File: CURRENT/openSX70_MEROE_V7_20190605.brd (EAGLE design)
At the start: 95.9 x 27.9 mm, 43 parts, among them J1 687106183722, Q1 5.8A/30V/35mΩ, Q2 5.8A/30V/35mΩ, U1 ATMEGA328P_TQFP, U2 TPS79501DCQ, Y1 CSTCE8M00G52Z-R0

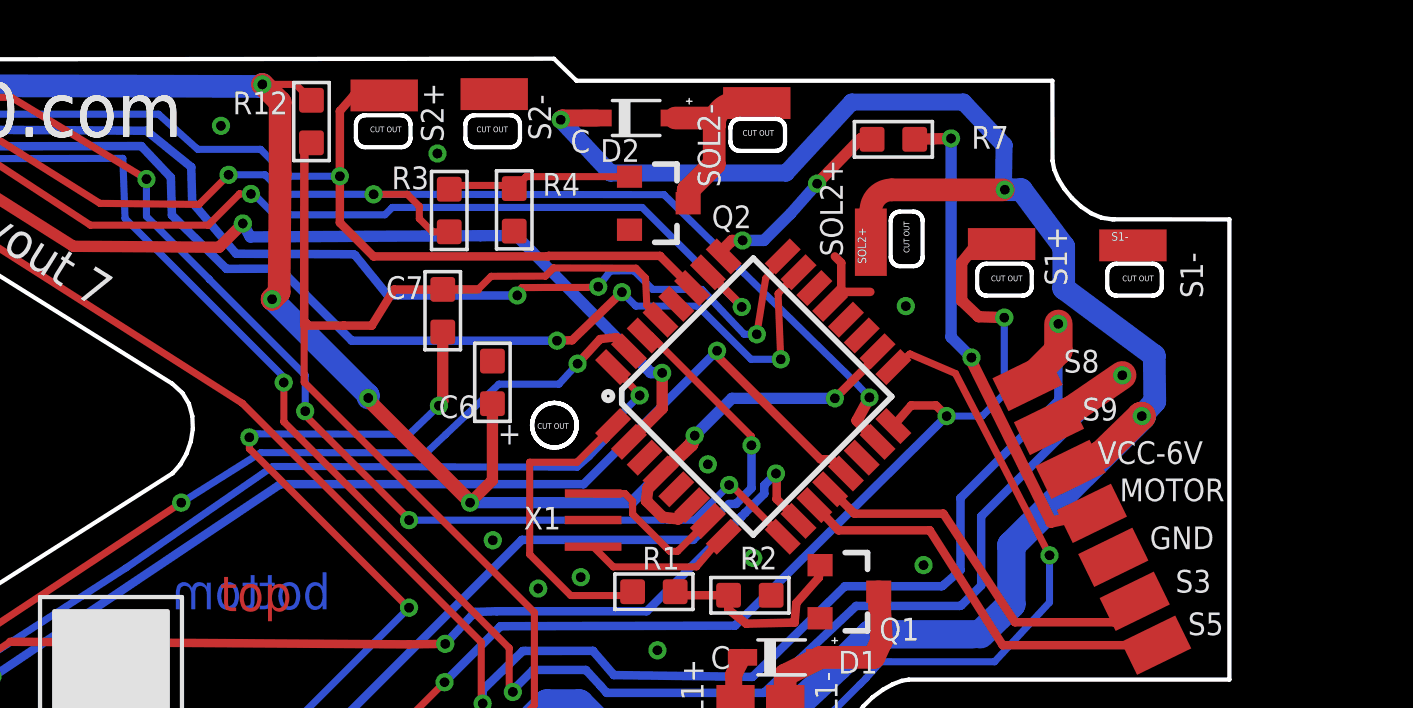
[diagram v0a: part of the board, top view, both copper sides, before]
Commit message: adding decoupling caps
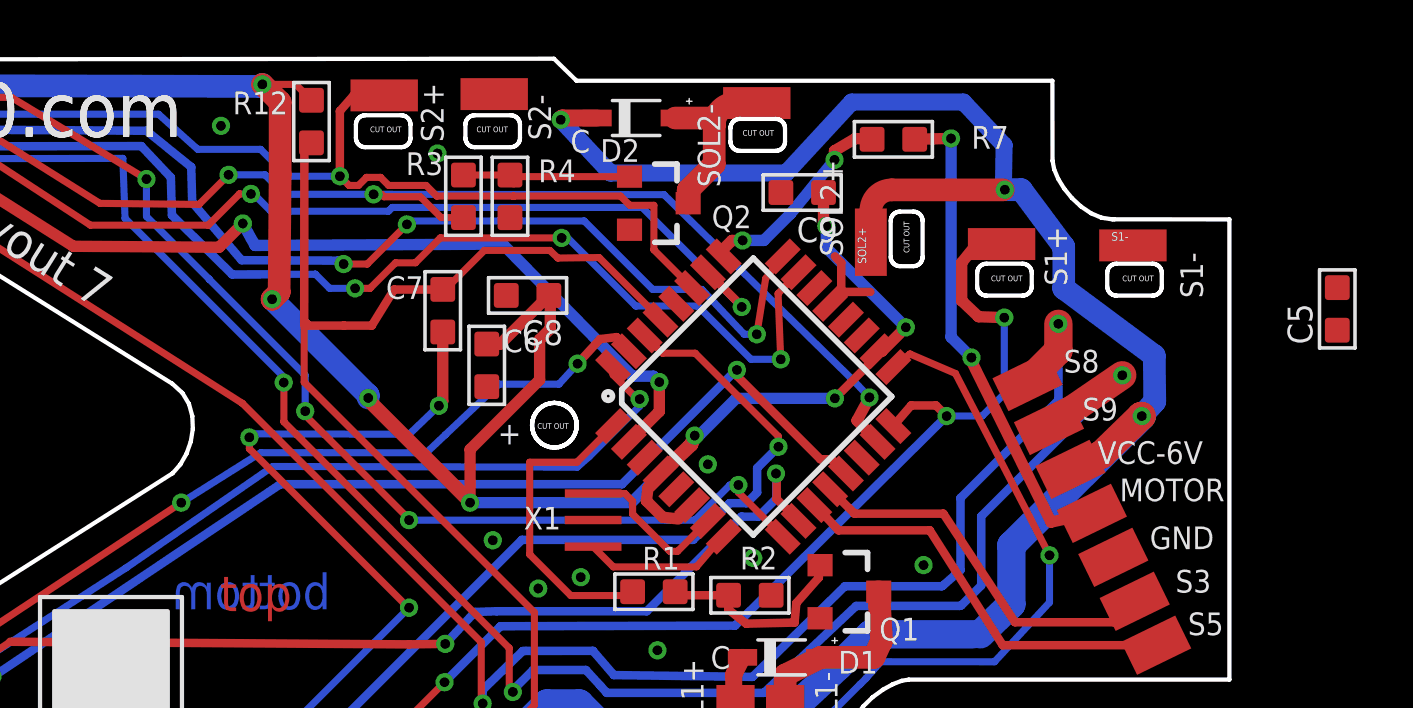
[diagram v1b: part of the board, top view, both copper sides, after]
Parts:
- added C5, C8, C9: 100nf, Seeed-Capacitor:C0603
- moved R3 0.72 mm to (70.5, 23.7)
- moved C6 0.64 mm to (71.4, 17.7), turned to 0 degrees
- moved R4 0.51 mm to (72.2, 23.7)
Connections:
- net 3.3V: now also C5.1, C8.1, C9.1
- net GND: now also C5.2, C8.2, C9.2
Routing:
- net 3.3V: track 159.8 -> 174.1 mm, vias 8 -> 10
- net RXD: track 121.9 -> 123.5 mm
- net N$3: track 7.18 -> 6.31 mm
- net RST: track 82.3 -> 81.5 mm
- net S8@2.5V: track 69.1 -> 69.8 mm
- net TCS3200_OE: track 100.5 -> 100.0 mm
- net GND: vias 21 -> 20
